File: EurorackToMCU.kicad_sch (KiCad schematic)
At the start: 26 parts, among them J30 CV_Scaled_Out1, J31 AudioToMCU1, J32 AudioToMCU2, J33 CV_In2, J48 CV_In1, J49 CV_Scaled_Out2, J50 AudioToMCU1, J51 AudioToMCU2, U1 MCP6004

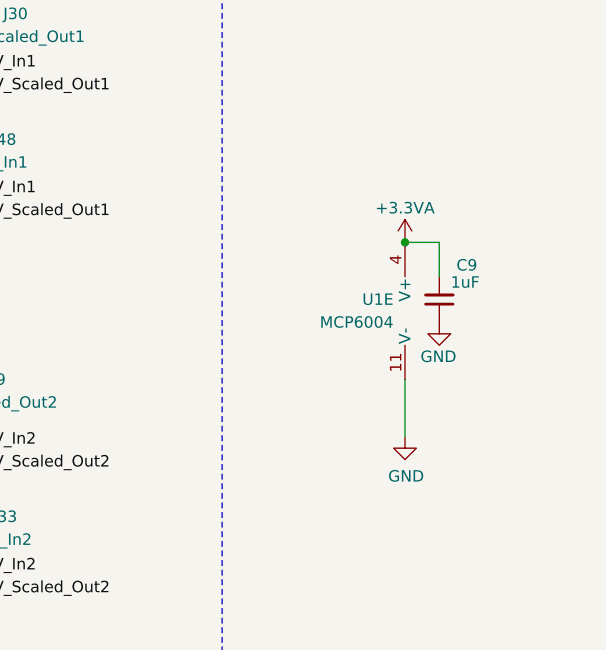
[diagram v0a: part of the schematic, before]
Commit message: Layout tweaks
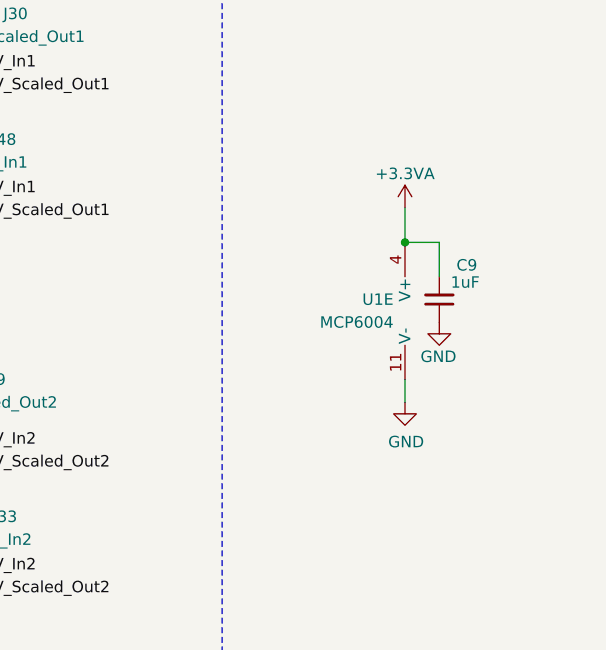
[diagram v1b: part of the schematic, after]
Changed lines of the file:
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@@
+    (stroke (width 0) (type default))
+  )
+  (wire (pts (xy 264.16 48.26) (xy 264.16 52.07))
     (stroke (width 0) (type default))
   )
@@
     (stroke (width 0) (type default))
   )
-  (wire (pts (xy 264.16 67.31) (xy 264.16 73.66))
+  (wire (pts (xy 264.16 67.31) (xy 264.16 69.85))
     (stroke (width 0) (type default))
   )
@@
     )
   )
-  (symbol (lib_id "power:GND") (at 264.16 73.66 0) (unit 1)
-    (in_bom yes) (on_board yes) (dnp no)
-    (property "Reference" "#PWR0103" (at 264.16 80.01 0)
-      (effects (font (size 1.27 1.27)) hide)
-    )
-    (property "Value" "GND" (at 264.287 78.0542 0)
-      (effects (font (size 1.27 1.27)))
-    )
-    (property "Footprint" "" (at 264.16 73.66 0)
-      (effects (font (size 1.27 1.27)) hide)
-    )
-    (property "Datasheet" "" (at 264.16 73.66 0)
+  (symbol (lib_id "power:GND") (at 264.16 69.85 0) (unit 1)
+    (in_bom yes) (on_board yes) (dnp no)
+    (property "Reference" "#PWR0103" (at 264.16 76.2 0)
+      (effects (font (size 1.27 1.27)) hide)
+    )
+    (property "Value" "GND" (at 264.287 74.2442 0)
+      (effects (font (size 1.27 1.27)))
+    )
+    (property "Footprint" "" (at 264.16 69.85 0)
+      (effects (font (size 1.27 1.27)) hide)
+    )
+    (property "Datasheet" "" (at 264.16 69.85 0)
       (effects (font (size 1.27 1.27)) hide)
     )
@@
     )
   )
-  (symbol (lib_id "power:+3.3VA") (at 264.16 52.07 0) (unit 1)
+  (symbol (lib_id "power:+3.3VA") (at 264.16 48.26 0) (unit 1)
     (in_bom yes) (on_board yes) (dnp no) (fields_autoplaced)
-    (property "Reference" "#PWR0102" (at 264.16 55.88 0)
-      (effects (font (size 1.27 1.27)) hide)
-    )
-    (property "Value" "+3.3VA" (at 264.16 48.26 0)
-      (effects (font (size 1.27 1.27)))
-    )
-    (property "Footprint" "" (at 264.16 52.07 0)
-      (effects (font (size 1.27 1.27)) hide)
-    )
-    (property "Datasheet" "" (at 264.16 52.07 0)
-      (effects (font (size 1.27 1.27)) hide)
-    )
+    (property "Reference" "#PWR0102" (at 264.16 52.07 0)
+      (effects (font (size 1.27 1.27)) hide)
+    )
+    (property "Value" "+3.3VA" (at 264.16 44.45 0)
+      (effects (font (size 1.27 1.27)))
+    )
+    (property "Footprint" "" (at 264.16 48.26 0)
+      (effects (font (size 1.27 1.27)) hide)
+    )
+    (property "Datasheet" "" (at 264.16 48.26 0)
+      (effects (font (size 1.27 1.27)) hide)
+    )

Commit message: Preparing for production
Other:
- note removed: "Full Scale: 7V"
- moved on the sheet: C2, R10, R3, R4, U1D
